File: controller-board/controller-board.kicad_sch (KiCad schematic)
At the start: 92 parts, among them J1 Conn_01x02, J2 Conn_01x02, J3 Conn_01x02, J4 Conn_01x02, J5 Conn_01x03, J6 Conn_01x02, J7 Conn_01x02, Q1 PMV45EN2, Q3 RQ3E120ATTB, U1 CAT4201, U2 PocketBeagle, U3 LTC3624, U4 CAT4201, U5 CAT4201, U6 CAT4201, U7 MCP4728, U8 ADC108S022

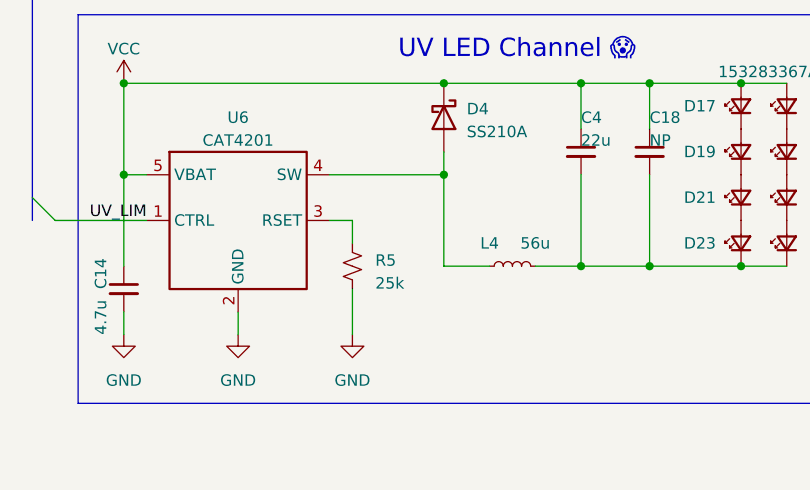
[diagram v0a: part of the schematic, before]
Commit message: Updated controller board and added BOM
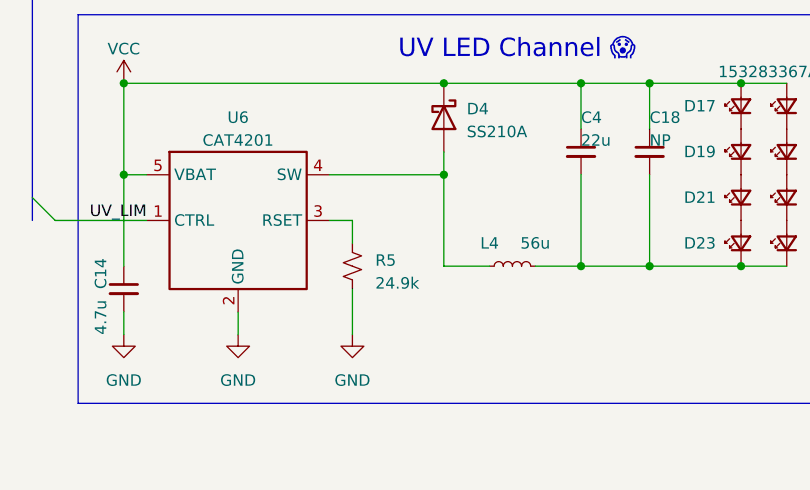
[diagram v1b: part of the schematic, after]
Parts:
- R5: value 25k -> 24.9k

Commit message: Updated main PCB. Added lots of LEDs and moved things around. Fixed some issues.
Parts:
- removed D15, D7: NP, LED_SMD:LED_Cree-XP, symbol Device:LED_Pad
- removed D16: XPEBBL-L1-0000-00201, LED_SMD:LED_Cree-XP, symbol Device:LED_Pad
- removed D17, D18, D19, D20, D21, D22, D23, D24: 153283367A212, LED_SMD:LED_PLCC_2835, symbol Device:LED_Small
- removed J7: Conn_01x02, TerminalBlock_Phoenix:TerminalBlock_Phoenix_PT-1,5-2-3.5-H_1x02_P3.50mm_Horizontal, symbol Connector_Generic:Conn_01x02
- removed Q3: RQ3E120ATTB, Package_SON:Diodes_PowerDI3333-8, symbol Transistor_FET:DMP3013SFV
- removed U8: ADC108S022, Package_SO:TSSOP-16_4.4x5mm_P0.65mm, symbol oresat-ics:ADC108S022
- added C25, C28, C29, C34, C35: 4.7u, Capacitor_SMD:C_0603_1608Metric, symbol Device:C_Small
- added C26, C30, C31, C36, C37, C40, C43: 22u, Capacitor_SMD:C_1210_3225Metric, symbol Device:C_Small
- added C27, C32, C33, C38, C39, C41, C42: NP, Capacitor_THT:C_Radial_D10.0mm_H16.0mm_P5.00mm, symbol Device:C_Small
- added C44: 1u, Capacitor_SMD:C_0603_1608Metric, symbol Device:C_Small
- added D15, D16, D17, D34, D35, D7: SS210A, Diode_SMD:D_SMA, symbol Device:D_Schottky
- added D18, D19, D20, D21, D22, D23, D28, D29, D30, D31, D32, D33, D36, D37, D38, D39, D40, D41: XPEBBL-L1-0000-00201, LED_SMD:LED_Cree-XP, symbol Device:LED_Pad
- added D25, D26, D27: XPEBRD-L1-0000-00501, LED_SMD:LED_Cree-XP, symbol Device:LED_Pad
- added L10, L11, L6, L7, L8, L9: 56u, Inductor_SMD:L_Wuerth_HCI-5040, symbol Device:L_Small
- added R14, R16, R17, R18, R19, R20: 10k, Resistor_SMD:R_0603_1608Metric, symbol Device:R_Small_US
- added U10, U11, U12, U13, U14, U15: CAT4201, Package_TO_SOT_SMD:TSOT-23-5, symbol oresat-ics:CAT4201
- added U16: DGD0216, Package_TO_SOT_SMD:TSOT-23-5, symbol oresat-ics:DGD0216
- added U8, U9: ADS1015IRUGR, Package_DFN_QFN:Texas_R-PUQFN-N10, symbol Analog_ADC:ADS1015IDGS
- C12, C13: value 4.7u -> 22u; footprint Capacitor_SMD:C_0603_1608Metric -> Capacitor_SMD:C_1210_3225Metric
- C18: value NP -> 22u; footprint Capacitor_THT:C_Radial_D10.0mm_H16.0mm_P5.00mm -> Capacitor_SMD:C_1210_3225Metric
- C2, C3, C4: value 22u -> 4.7u; footprint Capacitor_SMD:C_1210_3225Metric -> Capacitor_SMD:C_0603_1608Metric
- D11, D13, D9: value NP -> XPEBGR-L1-0000-00D01
- D14: value XPEBBL-L1-0000-00201 -> XPEBGR-L1-0000-00D01
- D5: value NP -> XPEBRD-L1-0000-00501
- J1, J6: footprint TerminalBlock_Phoenix:TerminalBlock_Phoenix_PT-1,5-2-3.5-H_1x02_P3.50mm_Horizontal -> TerminalBlock_Phoenix:TerminalBlock_Phoenix_PT-1,5-2-5.0-H_1x02_P5.00mm_Horizontal
- L1, L2, L3, L4: footprint Inductor_SMD:L_Bourns_SRN8040TA -> Inductor_SMD:L_Wuerth_HCI-5040
- Q1: value PMV45EN2 -> ~
- R10: value 10k -> 0
- R11: value 1k -> 10k
- R5: value 24.9k -> 10k
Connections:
- net +3.3V: now also U8.8 (VDD), U9.1 (ADDR), U9.8 (VDD)
- net BLUE_LIM: now also U11.1 (CTRL), U12.1 (CTRL), U13.1 (CTRL), U14.1 (CTRL); no longer U5.1 (CTRL)
- net GND: now also C2.2, C3.2, C4.2, J1.1 (Pin_1), R11.2, C25.2, C28.2, C29.2, C34.2, C35.2, C43.2, C44.2, D18.3 (PAD), D19.3 (PAD), D20.3 (PAD), D21.3 (PAD), D22.3 (PAD), D23.3 (PAD), D25.3 (PAD), D26.3 (PAD), D27.3 (PAD), D28.3 (PAD), D29.3 (PAD), D30.3 (PAD), D31.3 (PAD), D32.3 (PAD), D33.3 (PAD), D36.3 (PAD), D37.3 (PAD), D38.3 (PAD), D39.3 (PAD), D40.3 (PAD), D41.3 (PAD), R14.2, R16.2, R17.2, R18.2, R19.2, R20.2, U10.2 (GND), U11.2 (GND), U12.2 (GND), U13.2 (GND), U14.2 (GND), U15.2 (GND), U16.2 (GND), U8.1 (ADDR), U8.3 (GND), U9.3 (GND); no longer C12.2, C13.2, J1.2 (Pin_2), J6.2 (Pin_2), R10.2
- net GREEN_LIM: now also U5.1 (CTRL)
- net PHOTODIODE: now also U8.7 (AIN3)
- net RED_LIM: now also U10.1 (CTRL)
- net SCL1: now also U8.10 (SCL), U9.10 (SCL)
- net SDA1: now also U8.9 (SDA), U9.9 (SDA)
- net THERM1: now also U8.4 (AIN0)
- net THERM2: now also U8.5 (AIN1)
- net THERM3: now also U8.6 (AIN2)
- net UV_LIM: now also U15.1 (CTRL)
- net VCC: now also D11.2 (A), J6.2 (Pin_2), C25.1, C26.1, C27.1, C28.1, C29.1, C30.1, C31.1, C32.1, C33.1, C34.1, C35.1, C36.1, C37.1, C38.1, C39.1, C40.1, C41.1, C42.1, C43.1, C44.1, D15.1 (K), D16.1 (K), D17.1 (K), D18.2 (A), D20.2 (A), D25.2 (A), D28.2 (A), D30.2 (A), D34.1 (K), D35.1 (K), D36.2 (A), D38.2 (A), D7.1 (K), U10.5 (VBAT), U11.5 (VBAT), U12.5 (VBAT), U13.5 (VBAT), U14.5 (VBAT), U15.5 (VBAT), U16.5 (VCC); no longer D13.2 (A), R11.1
- net at D10.1 (K): now also C12.2, C16.2, L2.2; no longer D11.2 (A)
- net at D10.2 (A): now also D13.1 (K); no longer D9.1 (K)
- net at C17.2, L3.2: now also C13.2, D12.1 (K); no longer C3.2
- net at TP4.1: now also U9.7 (AIN3)
- net at D12.2 (A): now also D14.1 (K); no longer D11.1 (K)
- net at F1.1: now also J1.2 (Pin_2); no longer J1.1 (Pin_1)
- net at TP1.1: now also U9.4 (AIN0)
- net at Q1.3 (D): now also J6.1 (Pin_1); no longer R11.2
- net at C18.2, L4.2: now also C41.2, D19.1 (K); no longer C4.2
- net at TP3.1: now also U9.6 (AIN2)
- net at TP2.1: now also U9.5 (AIN1)
- net at D14.2 (A): now also D11.1 (K); no longer D13.1 (K)
- net at D8.2 (A): now also D6.1 (K)
- new net: D26.2 (A), D27.1 (K)
- new net: D25.1 (K), D27.2 (A)
- new net: D16.2 (A), L8.1, U12.4 (SW)
- new net: D15.2 (A), L7.1, U11.4 (SW)
- new net: C30.2, C32.2, D29.1 (K), L7.2
- new net: C31.2, C33.2, D31.1 (K), L8.2
- new net: D31.2 (A), D33.1 (K)
- new net: D37.2 (A), D40.1 (K)
- new net: D36.1 (K), D40.2 (A)
- new net: C40.2, C42.2, D21.1 (K), L11.2
- new net: R11.1, U16.3 (IN), U2.37 (PWM1A)
- new net: R10.1, U16.4 (OUT)
- new net: D19.2 (A), D22.1 (K)
- new net: R14.1, U10.3 (RSET)
- new net: D7.2 (A), L6.1, U10.4 (SW)
- new net: D17.2 (A), L11.1, U15.4 (SW)
- new net: D35.2 (A), L10.1, U14.4 (SW)
- new net: C37.2, C39.2, D39.1 (K), L10.2
- new net: Q1.1 (G), R10.2
- new net: D30.1 (K), D33.2 (A)
- new net: D29.2 (A), D32.1 (K)
- new net: D34.2 (A), L9.1, U13.4 (SW)
- new net: D28.1 (K), D32.2 (A)
- new net: R16.1, U11.3 (RSET)
- new net: D18.1 (K), D22.2 (A)
- new net: D21.2 (A), D23.1 (K)
- new net: D20.1 (K), D23.2 (A)
- new net: D38.1 (K), D41.2 (A)
- new net: R17.1, U12.3 (RSET)
- new net: D39.2 (A), D41.1 (K)
- new net: R20.1, U15.3 (RSET)
- new net: D13.2 (A), D9.1 (K)
- new net: C26.2, C27.2, D26.1 (K), L6.2
- new net: C36.2, C38.2, D37.1 (K), L9.2
- new net: R18.1, U13.3 (RSET)
- new net: R19.1, U14.3 (RSET)
- no-connect marks 1 -> 2
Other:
- note added: "UV LED Channel"
- note removed: "Only place 2 for now Extra pads if needed"
- note removed: "Only place 4 for now Extra pads if needed"
- note removed: "UV LED Channel 😱"
- moved on the sheet: C1, C11, C15, C21, C22, C23, C24, D1, D5, D6, D8, J1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

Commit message: Updated board design/layout and added step file
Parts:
- removed Q1: ~, Package_TO_SOT_SMD:SOT-23, symbol Device:Q_NMOS_GSD
- added C45, C46: 4.7u, Capacitor_SMD:C_0603_1608Metric, symbol Device:C_Small
- added C47, C48: 22u, Capacitor_SMD:C_1210_3225Metric, symbol Device:C_Small
- added C49, C50: NP, Capacitor_THT:C_Radial_D10.0mm_H16.0mm_P5.00mm, symbol Device:C_Small
- added D24, D42: NSR0320, Diode_SMD:D_SOD-323, symbol Device:D_Schottky
- added D43, D44, D45, D46, D47, D48: XPEBBL-L1-0000-00201, oresat-diodes:Cree-LED, symbol Device:LED_Pad
- added L12, L13: 56u, Inductor_SMD:L_Wuerth_HCI-5040, symbol Device:L_Small
- added Q1: SQS460EN, Package_SO:Vishay_PowerPAK_1212-8_Single, symbol Transistor_FET:SiS454DN
- added R21, R22: 10k, Resistor_SMD:R_0603_1608Metric, symbol Device:R_Small_US
- added TP8, TP9: TestPoint-MinTH, oresat-misc:TestPoint-MinTH, symbol oresat-misc:TestPoint-MinTH
- added U17, U18: CAT4201, Package_TO_SOT_SMD:TSOT-23-5, symbol oresat-ics:CAT4201
- C1: footprint Capacitor_SMD:C_1210_3225Metric -> oresat-diodes:Cree-LED
- D1, D15, D16, D17, D2, D3, D34, D35, D4, D7: value SS210A -> NSR0320; footprint Diode_SMD:D_SMA -> Diode_SMD:D_SOD-323
- D10, D11, D12, D13, D14, D18, D19, D20, D21, D22, D23, D25, D26, D27, D28, D29, D30, D31, D32, D33, D36, D37, D38, D39, D40, D41, D5, D6, D8, D9: footprint LED_SMD:LED_Cree-XP -> oresat-diodes:Cree-LED
- renumbered U16 to Q2
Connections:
- net +3.3V: now also TP8.1
- net GND: now also C45.2, C46.2, D43.3 (PAD), D44.3 (PAD), D45.3 (PAD), D46.3 (PAD), D47.3 (PAD), D48.3 (PAD), Q1.1 (S), Q1.2 (S), Q1.3 (S), R21.2, R22.2, TP9.1, U17.2 (GND), U18.2 (GND)
- net UV_LIM: now also U17.1 (CTRL), U18.1 (CTRL)
- net VCC: now also C45.1, C46.1, C47.1, C48.1, C49.1, C50.1, D24.1 (K), D42.1 (K), D43.2 (A), D45.2 (A), U17.5 (VBAT), U18.5 (VBAT)
- net at R10.2: now also Q1.4 (G)
- net at J6.1 (Pin_1): now also Q1.5 (D)
- new net: C47.2, C49.2, D44.1 (K), L12.2
- new net: D43.1 (K), D47.2 (A)
- new net: D44.2 (A), D47.1 (K)
- new net: C48.2, C50.2, D46.1 (K), L13.2
- new net: D46.2 (A), D48.1 (K)
- new net: R21.1, U17.3 (RSET)
- new net: D42.2 (A), L13.1, U18.4 (SW)
- new net: D45.1 (K), D48.2 (A)
- new net: R22.1, U18.3 (RSET)
- new net: D24.2 (A), L12.1, U17.4 (SW)

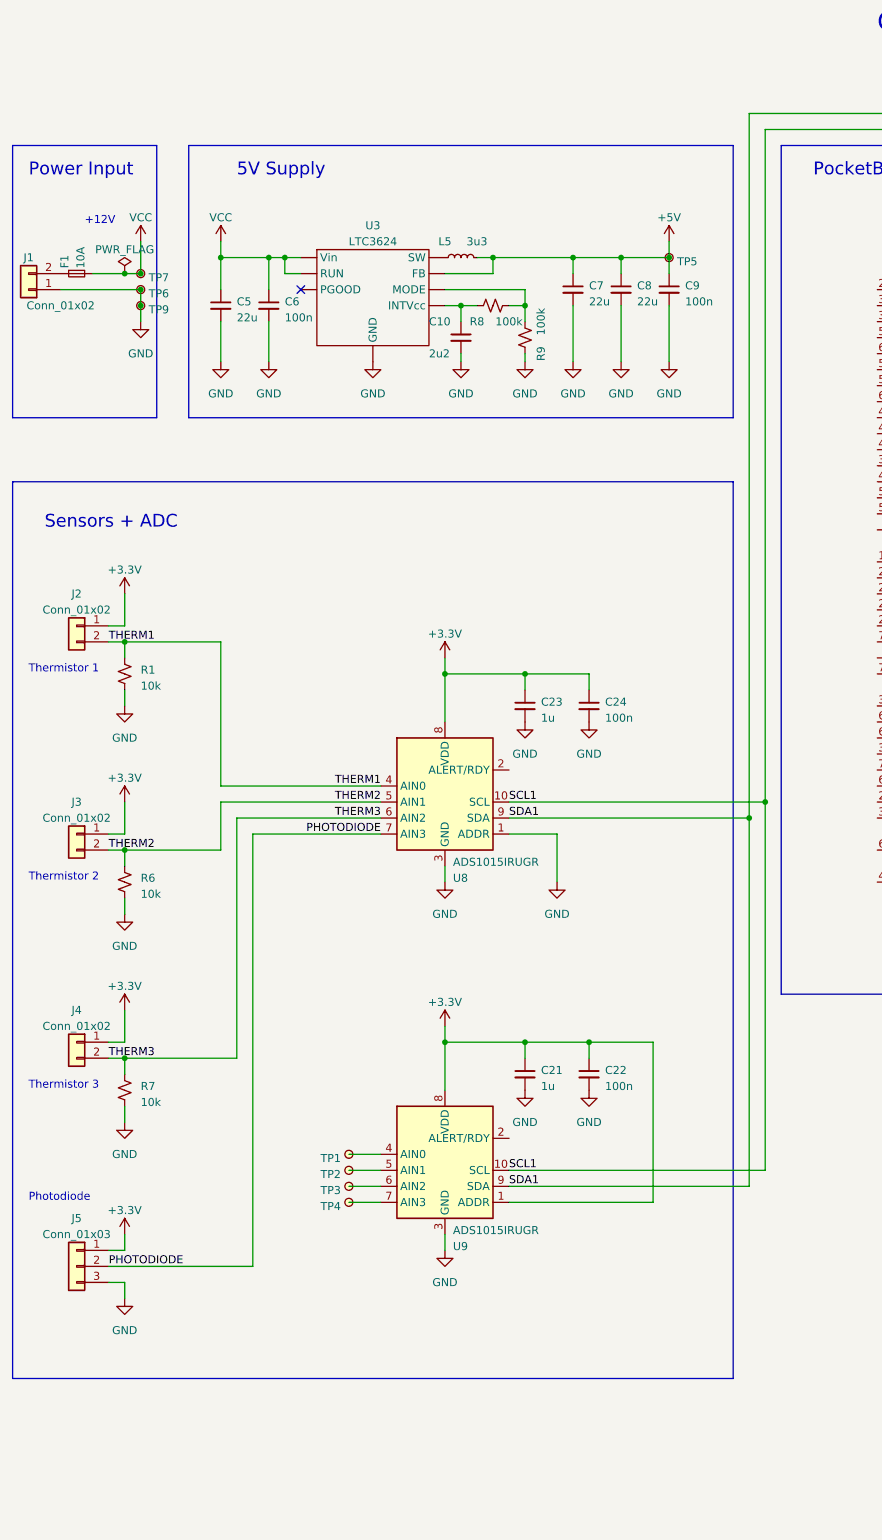
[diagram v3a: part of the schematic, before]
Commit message: Added GND stitching vias and on/off switch
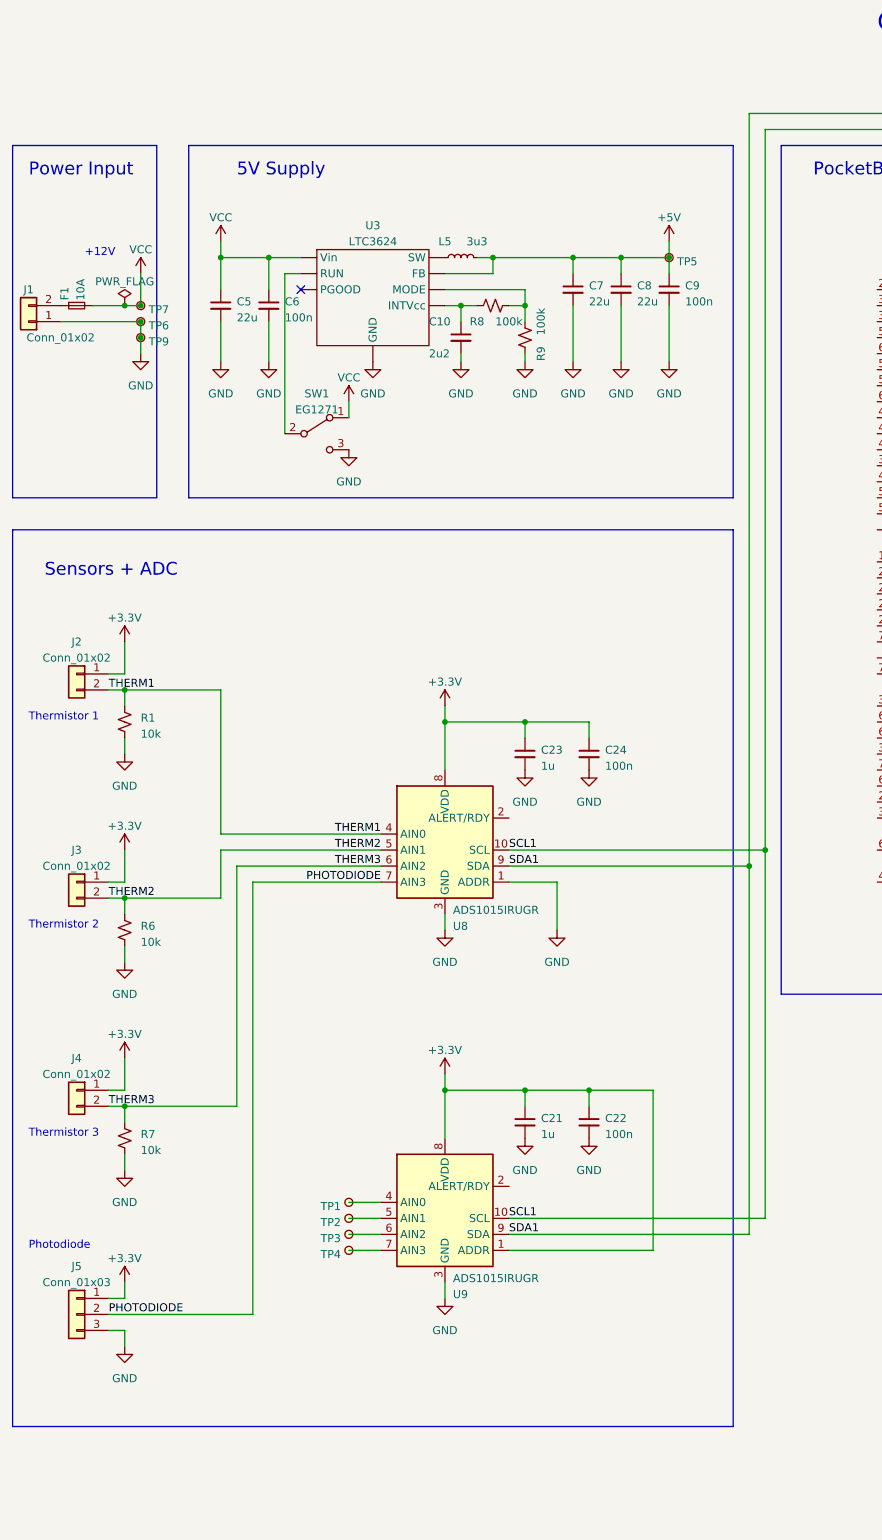
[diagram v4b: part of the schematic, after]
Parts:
- added SW1: EG1271, Button_Switch_THT:SW_E-Switch_EG1271_SPDT, symbol Switch:SW_SPDT
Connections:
- net GND: now also SW1.3 (C)
- net VCC: now also SW1.1 (A); no longer U3.3 (RUN)
- new net: SW1.2 (B), U3.3 (RUN)
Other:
- moved on the sheet: C21, C22, C23, C24, F1, J1, J2, J3, J4, J5, R1, R6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
